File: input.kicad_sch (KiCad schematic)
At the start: 5 parts, among them J5 Screw_Terminal_01x02, U4 EL817

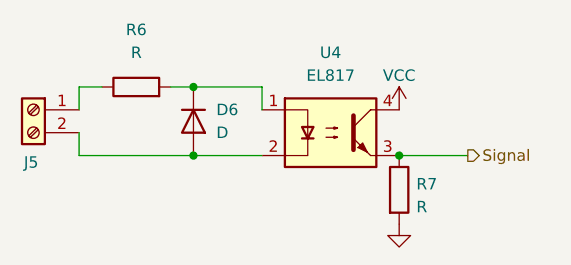
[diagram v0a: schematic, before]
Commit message: Schematic ready; PCB needs silkscreen
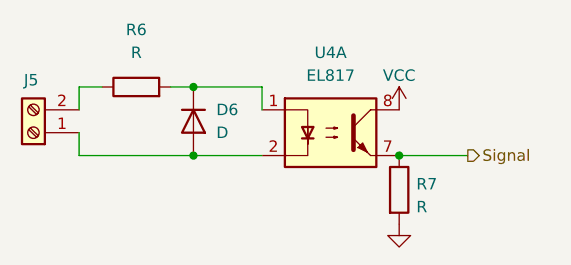
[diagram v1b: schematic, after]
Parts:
- D6: footprint (none) -> Diode_THT:D_DO-41_SOD81_P2.54mm_Vertical_AnodeUp
- J5: footprint (none) -> TerminalBlock_RND:TerminalBlock_RND_205-00001_1x02_P5.00mm_Horizontal
- R6, R7: footprint (none) -> Resistor_THT:R_Axial_DIN0204_L3.6mm_D1.6mm_P1.90mm_Vertical
- U4: footprint Package_DIP:DIP-4_W7.62mm -> Package_DIP:DIP-8_W7.62mm; symbol Isolator:EL817 -> Isolator:LTV-827
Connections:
- net Signal: now also U4.7; no longer U4.3
- net VCC: now also U4.8; no longer U4.4
- net at R6.1: now also J5.2 (Pin_2); no longer J5.1 (Pin_1)
- net at D6.2 (A), U4.2: now also J5.1 (Pin_1); no longer J5.2 (Pin_2)
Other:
- moved on the sheet: J5
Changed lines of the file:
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@@
 			)
 		)
-		(property "Footprint" ""
+		(property "Footprint" "Resistor_THT:R_Axial_DIN0204_L3.6mm_D1.6mm_P1.90mm_Vertical"
 			(at 130.81 93.218 90)
 			(effects
@@
 			)
 		)
-		(property "Footprint" ""
+		(property "Footprint" "Diode_THT:D_DO-41_SOD81_P2.54mm_Vertical_AnodeUp"
 			(at 137.16 95.25 0)
 			(effects
@@
 	(symbol
 		(lib_id "Connector:Screw_Terminal_01x02")
-		(at 119.38 93.98 0)
-		(mirror y)
+		(at 119.38 96.52 180)
 		(unit 1)
 		(exclude_from_sim no)
@@
 		(dnp no)
 		(property "Reference" "J5"
-			(at 119.126 99.822 0)
+			(at 119.126 90.678 0)
 			(effects
 				(font
@@
 		)
 		(property "Value" "Screw_Terminal_01x02"
-			(at 119.38 100.33 0)
-			(effects
-				(font
-					(size 1.27 1.27)
-				)
-				(hide yes)
-			)
-		)
-		(property "Footprint" ""
-			(at 119.38 93.98 0)
+			(at 119.38 90.17 0)
+			(effects
+				(font
+					(size 1.27 1.27)
+				)
+				(hide yes)
+			)
+		)
+		(property "Footprint" "TerminalBlock_RND:TerminalBlock_RND_205-00001_1x02_P5.00mm_Horizontal"
+			(at 119.38 96.52 0)
 			(effects
 				(font
@@
 		)
 		(property "Datasheet" "~"
-			(at 119.38 93.98 0)
+			(at 119.38 96.52 0)
 			(effects
 				(font
@@
 		)
 		(property "Description" "Generic screw terminal, single row, 01x02, script generated (kicad-library-utils/schlib/autogen/connector/)"
-			(at 119.38 93.98 0)
+			(at 119.38 96.52 0)
 			(effects
 				(font
@@
 			)
 		)
-		(property "Footprint" ""
+		(property "Footprint" "Resistor_THT:R_Axial_DIN0204_L3.6mm_D1.6mm_P1.90mm_Vertical"
 			(at 158.242 102.87 90)
 			(effects
@@
 	)
 	(symbol
-		(lib_id "Isolator:EL817")
+		(lib_id "Isolator:LTV-827")
 		(at 152.4 96.52 0)
 		(unit 1)
@@
 			)
 		)
-		(property "Footprint" "Package_DIP:DIP-4_W7.62mm"
+		(property "Footprint" "Package_DIP:DIP-8_W7.62mm"
 			(at 147.32 101.6 0)
 			(effects
@@
 			)
 		)
-		(property "Datasheet" "http://www.everlight.com/file/ProductFile/EL817.pdf"
+		(property "Datasheet" "http://optoelectronics.liteon.com/upload/download/DS-70-96-0016/LTV-8X7%20series%20201610%20.pdf"
 			(at 152.4 96.52 0)
 			(effects
@@
 			)
 		)
-		(property "Description" "DC Optocoupler, Vce 35V, DIP-4"
+		(property "Description" "Dual DC Optocoupler, Vce 35V, CTR 50%, DIP-8"
 			(at 152.4 96.52 0)
 			(effects
@@
 		(pin "4"
 		)
+		(pin "7"
+		)
+		(pin "6"
+		)
+		(pin "5"
+		)
+		(pin "8"
+		)
 		(instances
 			(project "SolderTestPCB"
@@
 				)
 				(path "/3f231ef2-6b13-4d44-9a8c-c6a44054681e/7544685c-37e6-4b42-bc38-fa5126aeab4a"
-					(reference "U5")
-					(unit 1)
-				)
+					(reference "U4")
+					(unit 1)
+				)
